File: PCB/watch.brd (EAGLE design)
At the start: 81.1 x 53.1 mm, 58 parts, among them IC1 ISL1209, J2 USB-MICROB, Q1 32.768 KHz, T1 BC850, U2 MKL27Z256VLH4

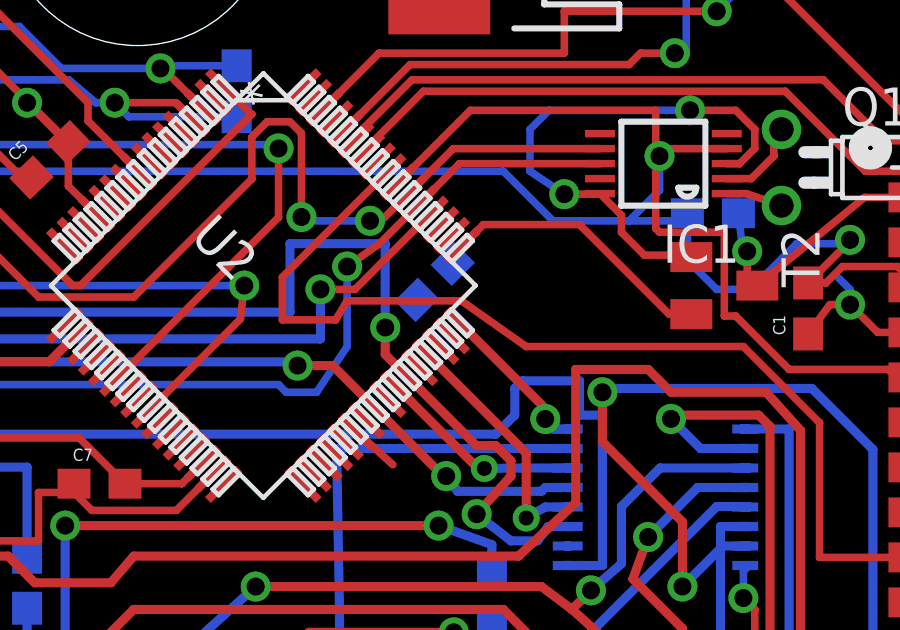
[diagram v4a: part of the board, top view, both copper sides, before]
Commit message: finished last decoupling cap
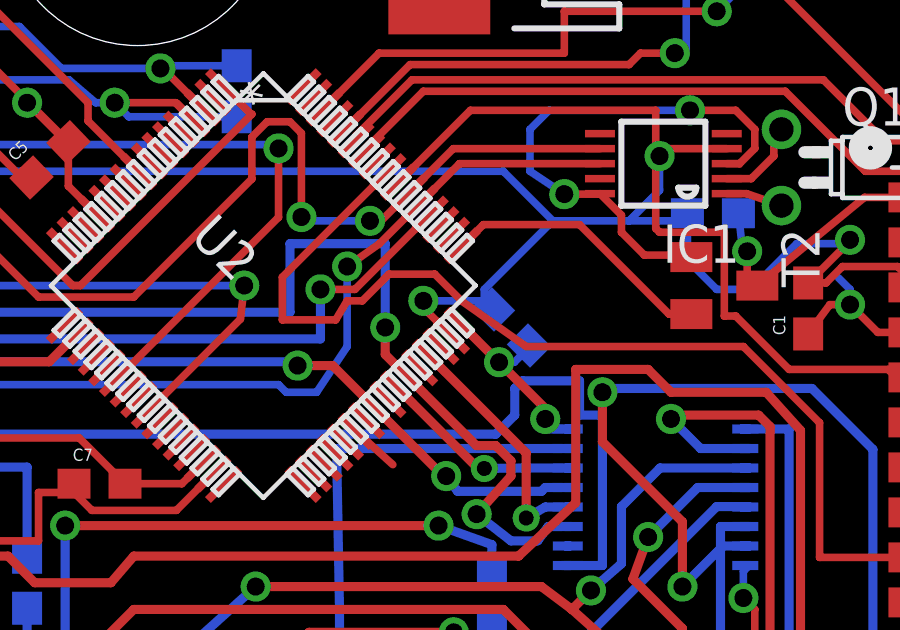
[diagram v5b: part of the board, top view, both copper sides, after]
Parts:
- moved C8 2.96 mm to (58.9, 40.5), turned to 225 degrees
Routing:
- net GND: track 133.0 -> 140.7 mm, vias 13 -> 14
- net V+: track 107.6 -> 108.8 mm, vias 12 -> 13
- net PTC11: track 34.0 -> 34.7 mm
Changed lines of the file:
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@@
 <element name="C6" library="SparkFun" package="0603" value=".1uf" x="49.784" y="48.387" rot="MR90"/>
 <element name="C7" library="SparkFun" package="0603" value=".1uf" x="45.212" y="35.306"/>
-<element name="C8" library="SparkFun" package="0603" value=".1uf" x="56.388" y="42.037" rot="MR135"/>
+<element name="C8" library="SparkFun" package="0603" value=".1uf" x="58.928" y="40.513" rot="MR225"/>
 <element name="COMPCAP" library="SparkFun" package="0603" value=".1uf" x="18.796" y="41.402" rot="R225"/>
 <element name="DISP1" library="SparkFun-Displays" package="DIL12" value="7-SEGMENT-4DIGIT-COUNTER-HP-BUBBLE" x="44.069" y="25.273">
@@
 <wire x1="35.56" y1="31.877" x2="35.814" y2="31.623" width="0.254" layer="1"/>
 <wire x1="35.814" y1="31.623" x2="36.449" y2="31.623" width="0.254" layer="1"/>
-<wire x1="60.325" y1="44.069" x2="56.94858125" y2="40.23061875" width="0" layer="19" extent="1-16"/>
-<wire x1="55.786959375" y1="41.43595625" x2="15.174" y2="44.239" width="0" layer="19" extent="1-1"/>
+<wire x1="58.326959375" y1="41.114040625" x2="58.039" y2="41.402" width="0.254" layer="16"/>
+<wire x1="58.039" y1="41.402" x2="56.007" y2="41.402" width="0.254" layer="16"/>
+<via x="56.007" y="41.402" extent="1-16" drill="0.6"/>
+<wire x1="56.007" y1="41.402" x2="56.007" y2="41.1722" width="0.254" layer="1"/>
+<wire x1="56.007" y1="41.1722" x2="56.94858125" y2="40.23061875" width="0.254" layer="1"/>
+<wire x1="58.039" y1="41.402" x2="58.039" y2="41.783" width="0.254" layer="16"/>
+<wire x1="58.039" y1="41.783" x2="60.325" y2="44.069" width="0.254" layer="16"/>
 </signal>
 <signal name="V+">
@@
 <wire x1="60.116" y1="37.129" x2="60.071" y2="37.465" width="0.3048" layer="16"/>
 <via x="60.071" y="37.465" extent="1-16" drill="0.6"/>
-<wire x1="60.071" y1="37.81530625" x2="57.302134375" y2="40.584171875" width="0.3048" layer="1"/>
+<wire x1="60.071" y1="37.81530625" x2="58.531653125" y2="39.354653125" width="0.3048" layer="1"/>
+<wire x1="58.531653125" y1="39.354653125" x2="57.302134375" y2="40.584171875" width="0.3048" layer="1"/>
 <wire x1="60.071" y1="37.81530625" x2="60.071" y2="37.465" width="0.3048" layer="1"/>
 <wire x1="19.397040625" y1="42.003040625" x2="20.0687375" y2="42.003040625" width="0.3048" layer="1"/>
@@
 <wire x1="31.115" y1="36.83" x2="30.353" y2="36.068" width="0.254" layer="1"/>
 <wire x1="30.353" y1="36.068" x2="30.353" y2="35.433" width="0.254" layer="1"/>
+<wire x1="59.52904375" y1="39.91195625" x2="59.52904375" y2="39.84404375" width="0.254" layer="16"/>
+<via x="58.531653125" y="39.354653125" extent="1-16" drill="0.6"/>
+<wire x1="59.52904375" y1="39.84404375" x2="59.039653125" y2="39.354653125" width="0.254" layer="16"/>
+<wire x1="59.039653125" y1="39.354653125" x2="58.531653125" y2="39.354653125" width="0.254" layer="16"/>
 <wire x1="63.666" y1="12.954" x2="63.666" y2="16.002" width="0" layer="19" extent="1-1"/>
 <wire x1="43.649" y1="13.335" x2="63.666" y2="12.954" width="0" layer="19" extent="1-1"/>
@@
 <wire x1="41.822" y1="16.002" x2="43.649" y2="13.335" width="0" layer="19" extent="1-1"/>
 <wire x1="46.062" y1="35.306" x2="41.822" y2="16.002" width="0" layer="19" extent="1-1"/>
-<wire x1="57.302134375" y1="40.584171875" x2="60.706" y2="44.958" width="0" layer="19" extent="1-16"/>
-<wire x1="56.98904375" y1="42.638040625" x2="20.32" y2="51.308" width="0" layer="19" extent="1-16"/>
 </signal>
 <signal name="PTA19">
@@
 <wire x1="69.215" y1="37.338" x2="69.215" y2="32.85" width="0.254" layer="1"/>
 <wire x1="69.215" y1="32.85" x2="72.51" y2="32.85" width="0.254" layer="1"/>
-<wire x1="57.277" y1="41.402" x2="53.467" y2="41.402" width="0.254" layer="1"/>
+<wire x1="53.467" y1="41.402" x2="53.975" y2="41.402" width="0.254" layer="1"/>
+<wire x1="53.975" y1="41.402" x2="54.864" y2="42.291" width="0.254" layer="1"/>
+<wire x1="54.864" y1="42.291" x2="56.388" y2="42.291" width="0.254" layer="1"/>
+<wire x1="56.388" y1="42.291" x2="57.277" y2="41.402" width="0.254" layer="1"/>
 </signal>
 <signal name="PTC4">

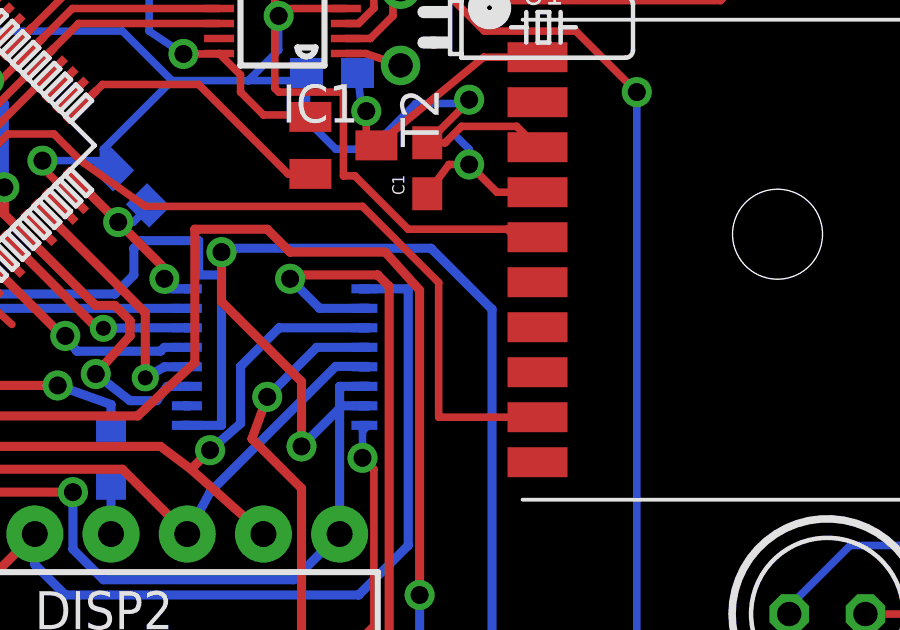
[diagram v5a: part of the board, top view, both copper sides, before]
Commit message: added gps tx resistor
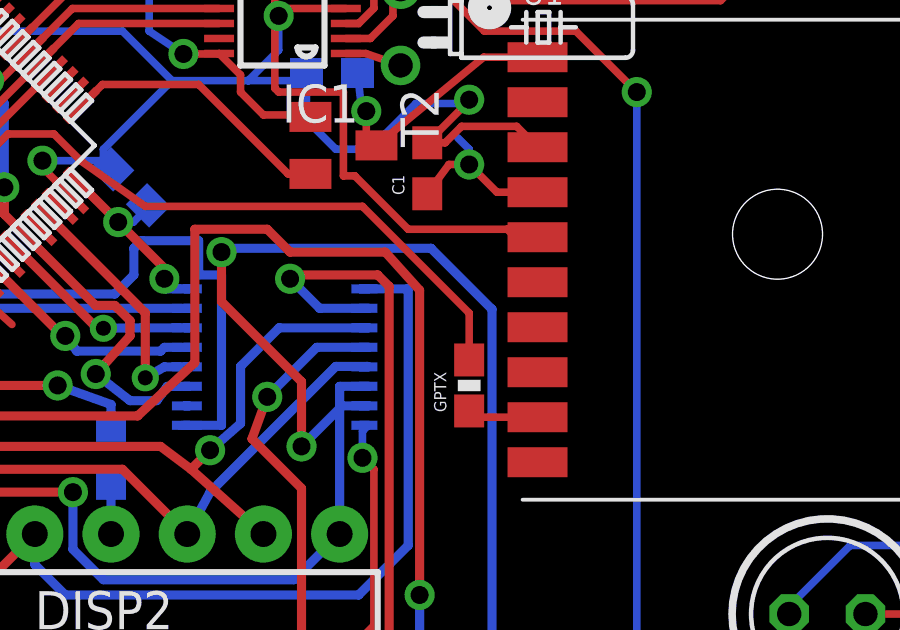
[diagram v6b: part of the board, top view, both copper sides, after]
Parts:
- added GPTX: 330, SparkFun-Resistors:0603-RES
- C2: value .1uf -> 1uf
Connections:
- new net N$30: GPTX.1, U1.P$9
- net PTC11: now also GPTX.2; no longer U1.P$9
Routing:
- net PTC11: track 34.7 -> 29.9 mm
- net N$30: track 0.00 -> 2.49 mm
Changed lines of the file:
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@@
 <element name="12CR2" library="SparkFun-Resistors" package="0603-RES" value="10K" x="26.162" y="42.926" rot="R90"/>
 <element name="C1" library="SparkFun" package="0603" value=".1uf" x="68.834" y="41.148" rot="R90"/>
-<element name="C2" library="SparkFun" package="0603" value=".1uf" x="65.659" y="44.323" rot="MR0"/>
+<element name="C2" library="SparkFun" package="0603" value="1uf" x="65.659" y="44.323" rot="MR0"/>
 <element name="C3" library="SparkFun-Capacitors" package="0603-CAP" value="4.7uF" x="70.358" y="54.991" rot="R90">
 <attribute name="PROD_ID" value="CAP-00810" x="70.358" y="54.991" size="1.778" layer="27" rot="R90" display="off"/>
@@
 <attribute name="CPU" value="ARM Cortex-M0+" x="50.673" y="41.91" size="1.778" layer="27" rot="R315" display="off"/>
 </element>
+<element name="GPTX" library="SparkFun-Resistors" package="0603-RES" value="330" x="70.231" y="33.909" rot="R90"/>
 </elements>
 <signals>
@@
 </signal>
 <signal name="PTC11">
-<contactref element="U1" pad="P$9"/>
 <contactref element="U2" pad="56"/>
-<wire x1="69.215" y1="37.338" x2="66.675" y2="39.878" width="0.254" layer="1"/>
+<wire x1="70.231" y1="36.322" x2="66.675" y2="39.878" width="0.254" layer="1"/>
 <wire x1="66.675" y1="39.878" x2="59.436" y2="39.878" width="0.254" layer="1"/>
 <wire x1="59.436" y1="39.878" x2="57.277" y2="41.402" width="0.254" layer="1"/>
@@
 <wire x1="51.308" y1="40.767" x2="51.308" y2="42.1914625" width="0.254" layer="1"/>
 <wire x1="51.308" y1="42.1914625" x2="54.827246875" y2="45.710709375" width="0.254" layer="1"/>
-<wire x1="69.215" y1="37.338" x2="69.215" y2="32.85" width="0.254" layer="1"/>
-<wire x1="69.215" y1="32.85" x2="72.51" y2="32.85" width="0.254" layer="1"/>
 <wire x1="53.467" y1="41.402" x2="53.975" y2="41.402" width="0.254" layer="1"/>
 <wire x1="53.975" y1="41.402" x2="54.864" y2="42.291" width="0.254" layer="1"/>
 <wire x1="54.864" y1="42.291" x2="56.388" y2="42.291" width="0.254" layer="1"/>
 <wire x1="56.388" y1="42.291" x2="57.277" y2="41.402" width="0.254" layer="1"/>
+<contactref element="GPTX" pad="2"/>
+<wire x1="70.231" y1="34.759" x2="70.231" y2="36.322" width="0.254" layer="1"/>
 </signal>
 <signal name="PTC4">
@@
 <wire x1="61.214" y1="43.942" x2="64.196" y2="40.96" width="0.254" layer="1"/>
 </signal>
+<signal name="N$30">
+<contactref element="GPTX" pad="1"/>
+<contactref element="U1" pad="P$9"/>
+<wire x1="72.51" y1="32.85" x2="70.231" y2="32.85" width="0.254" layer="1"/>
+<wire x1="70.231" y1="32.85" x2="70.231" y2="33.059" width="0.254" layer="1"/>
+</signal>
 </signals>

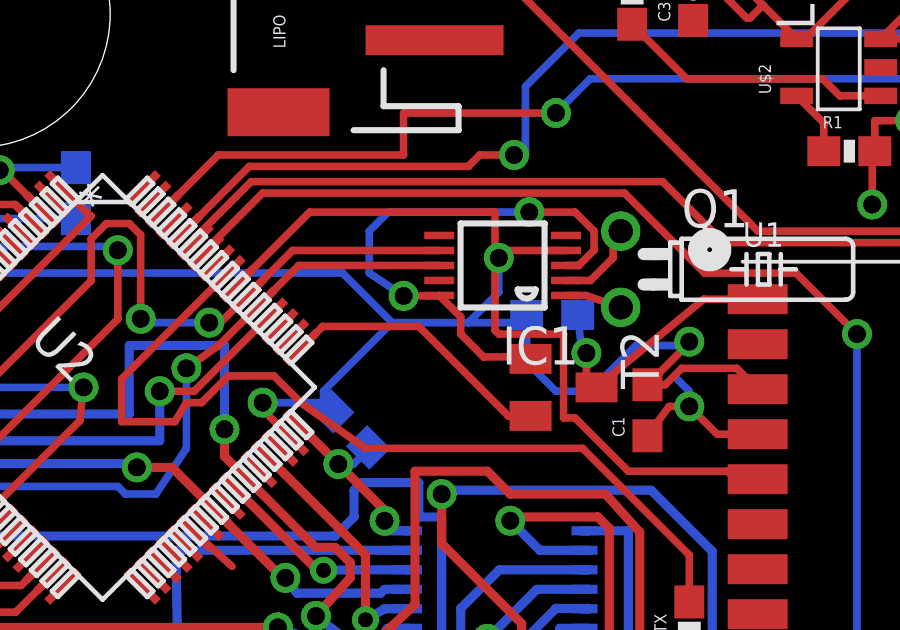
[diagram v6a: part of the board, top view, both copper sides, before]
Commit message: altered values on gps caps
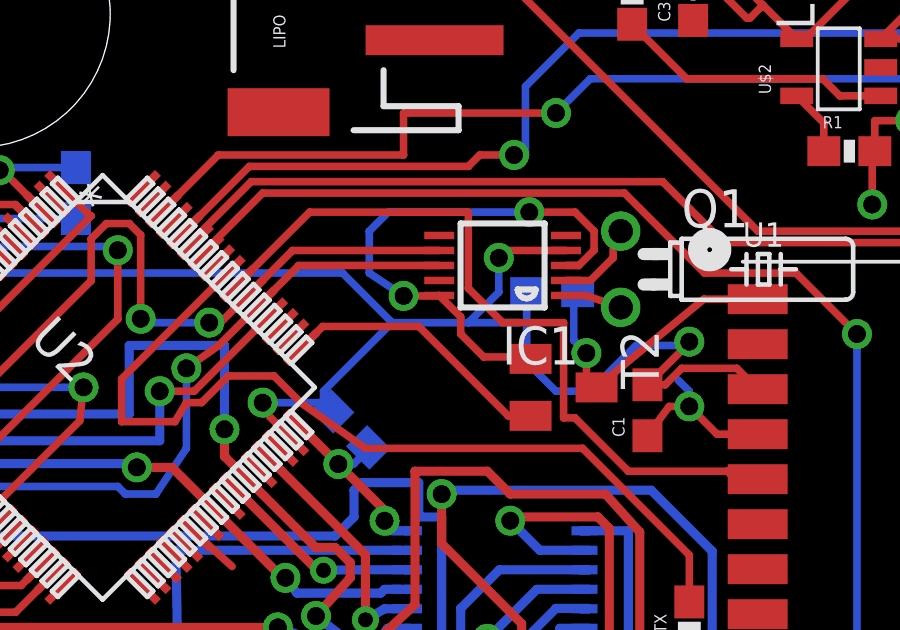
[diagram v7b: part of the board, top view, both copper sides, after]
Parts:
- C1: value .1uf -> 1uf
- moved C2 0.76 mm to (65.7, 45.1)
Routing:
- net N$6: track 9.05 -> 10.2 mm
- net PTC10: track 26.2 -> 25.6 mm
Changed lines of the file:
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@@
 <elements>
 <element name="12CR2" library="SparkFun-Resistors" package="0603-RES" value="10K" x="26.162" y="42.926" rot="R90"/>
-<element name="C1" library="SparkFun" package="0603" value=".1uf" x="68.834" y="41.148" rot="R90"/>
-<element name="C2" library="SparkFun" package="0603" value="1uf" x="65.659" y="44.323" rot="MR0"/>
+<element name="C1" library="SparkFun" package="0603" value="1uf" x="68.834" y="41.148" rot="R90"/>
+<element name="C2" library="SparkFun" package="0603" value="1uf" x="65.659" y="45.085" rot="MR0"/>
 <element name="C3" library="SparkFun-Capacitors" package="0603-CAP" value="4.7uF" x="70.358" y="54.991" rot="R90">
 <attribute name="PROD_ID" value="CAP-00810" x="70.358" y="54.991" size="1.778" layer="27" rot="R90" display="off"/>
@@
 <wire x1="60.325" y1="44.069" x2="62.865" y2="44.069" width="0.254" layer="16"/>
 <wire x1="62.865" y1="44.069" x2="64.555" y2="44.069" width="0.254" layer="16"/>
-<wire x1="64.555" y1="44.069" x2="64.809" y2="44.323" width="0.254" layer="16"/>
 <wire x1="66.1211" y1="46.474" x2="64.127" y2="46.474" width="0.254" layer="1"/>
 <wire x1="64.127" y1="46.474" x2="63.881" y2="46.228" width="0.254" layer="1"/>
@@
 <wire x1="63.881" y1="46.228" x2="63.881" y2="45.085" width="0.254" layer="16"/>
 <wire x1="63.881" y1="45.085" x2="62.865" y2="44.069" width="0.254" layer="16"/>
-<wire x1="64.809" y1="44.323" x2="64.809" y2="42.76" width="0.254" layer="16"/>
+<wire x1="64.809" y1="45.085" x2="64.809" y2="42.76" width="0.254" layer="16"/>
 <wire x1="64.809" y1="42.76" x2="65.786" y2="41.783" width="0.254" layer="16"/>
 <wire x1="65.786" y1="41.783" x2="66.929" y2="41.783" width="0.254" layer="16"/>
@@
 <wire x1="58.039" y1="41.402" x2="58.039" y2="41.783" width="0.254" layer="16"/>
 <wire x1="58.039" y1="41.783" x2="60.325" y2="44.069" width="0.254" layer="16"/>
+<wire x1="63.881" y1="45.085" x2="64.809" y2="45.085" width="0" layer="19" extent="16-16"/>
 </signal>
 <signal name="V+">
@@
 <wire x1="67.14" y1="41.91" x2="70.715" y2="44.85" width="0.254" layer="1"/>
 <wire x1="70.715" y1="44.85" x2="72.51" y2="44.85" width="0.254" layer="1"/>
-<wire x1="66.509" y1="44.323" x2="66.636" y2="43.219" width="0.254" layer="16"/>
 <wire x1="66.636" y1="43.219" x2="66.802" y2="43.053" width="0.254" layer="16"/>
 <via x="66.802" y="43.053" extent="1-16" drill="0.6"/>
 <wire x1="66.802" y1="43.053" x2="66.802" y2="42.248" width="0.254" layer="1"/>
 <wire x1="66.802" y1="42.248" x2="67.14" y2="41.91" width="0.254" layer="1"/>
+<wire x1="66.382" y1="43.473" x2="66.802" y2="43.053" width="0.254" layer="16"/>
+<wire x1="66.382" y1="43.473" x2="66.382" y2="44.958" width="0.254" layer="16"/>
+<wire x1="66.382" y1="44.958" x2="66.509" y2="45.085" width="0.254" layer="16"/>
 </signal>
 <signal name="PTB3">
@@
 <contactref element="U2" pad="55"/>
 <wire x1="55.18081875" y1="45.357140625" x2="57.575678125" y2="47.752" width="0.254" layer="1"/>
-<wire x1="57.575678125" y1="47.752" x2="63.754" y2="47.752" width="0.254" layer="1"/>
-<wire x1="63.754" y1="47.752" x2="63.754" y2="43.815" width="0.254" layer="1"/>
-<wire x1="63.754" y1="43.815" x2="63.881" y2="43.688" width="0.254" layer="1"/>
 <wire x1="72.009" y1="38.608" x2="72.251" y2="38.85" width="0.254" layer="1"/>
 <wire x1="72.251" y1="38.85" x2="72.51" y2="38.85" width="0.254" layer="1"/>
@@
 <wire x1="68.199" y1="39.116" x2="66.421" y2="40.894" width="0.254" layer="1"/>
 <wire x1="66.421" y1="40.894" x2="66.04" y2="40.894" width="0.254" layer="1"/>
-<wire x1="66.04" y1="40.894" x2="66.04" y2="43.688" width="0.254" layer="1"/>
-<wire x1="66.04" y1="43.688" x2="63.881" y2="43.688" width="0.254" layer="1"/>
+<wire x1="66.04" y1="40.894" x2="66.04" y2="44.069" width="0.254" layer="1"/>
+<wire x1="62.865" y1="45.212" x2="62.865" y2="47.752" width="0.254" layer="1"/>
+<wire x1="62.865" y1="47.752" x2="57.575678125" y2="47.752" width="0.254" layer="1"/>
+<wire x1="62.865" y1="45.212" x2="64.008" y2="44.069" width="0.254" layer="1"/>
+<wire x1="64.008" y1="44.069" x2="66.04" y2="44.069" width="0.254" layer="1"/>
 </signal>
 <signal name="PTC11">
